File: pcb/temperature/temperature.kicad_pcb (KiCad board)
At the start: 2 copper layers, 15 x 15 mm, 4 parts, among them J1 SM04B-GHS-TB, U1 TMP100

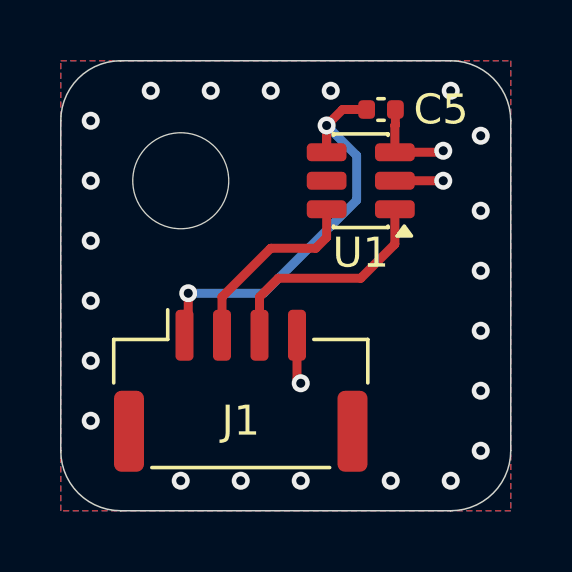
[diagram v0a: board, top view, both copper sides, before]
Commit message: major overhaul for rflink. Python scripts for gr-dvbs rx/tx. Tested in loopback mode. Have not added mpeg pipeline yet. See readme for details. Exported pcb files for fab
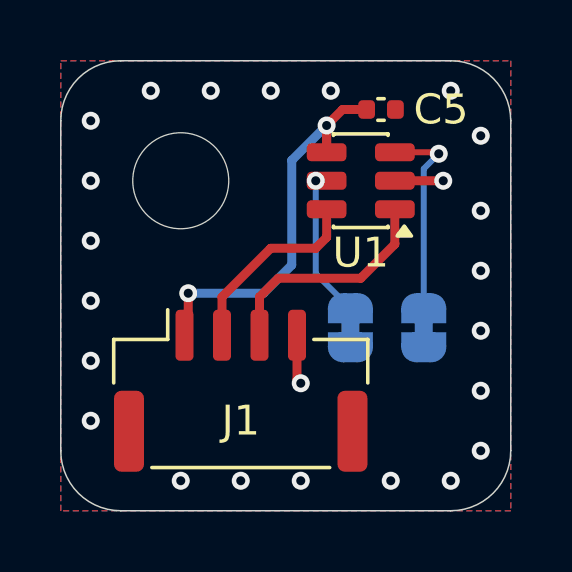
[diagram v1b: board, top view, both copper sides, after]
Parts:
- added JP1: SolderJumper_2_Bridged, Jumper:SolderJumper-2_P1.3mm_Bridged_RoundedPad1.0x1.5mm, B.Cu at (106.7, 88.9)
- added JP2: SolderJumper_2_Bridged, Jumper:SolderJumper-2_P1.3mm_Bridged_RoundedPad1.0x1.5mm, B.Cu at (109.1, 88.9)
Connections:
- U1 pad 3: GND -> Net-(JP2-B)
- U1 pad 5: unconnected-(U1-ADD0-Pad5) -> Net-(JP1-B)
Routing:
- net Net-(JP2-B): track 0.00 -> 6.84 mm, vias 0 -> 1
- net Net-(JP1-B): track 0.00 -> 5.09 mm, vias 0 -> 1
- net GND: track 6.33 -> 3.26 mm, vias 25 -> 24
- net +3V3_SBC: track 14.6 -> 13.8 mm
